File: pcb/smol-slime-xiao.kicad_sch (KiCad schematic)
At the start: 12 parts, among them J1 Conn_01x02, J2 Conn_01x02, U1 ICM-45686, U3 1532H, U4 XIAO-nRF52840-SMD

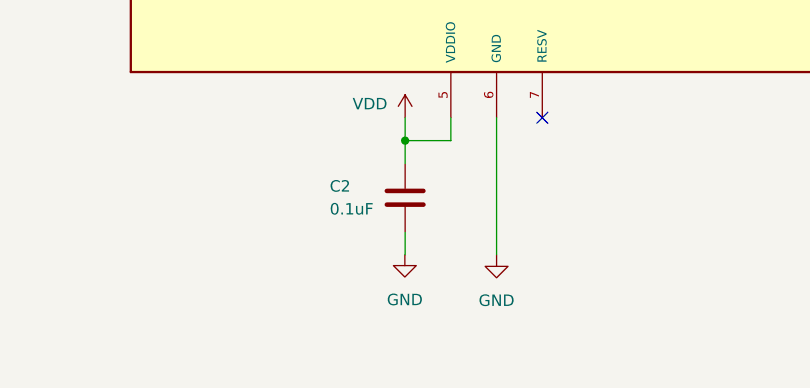
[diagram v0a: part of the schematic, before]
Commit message: Fix C2 GND connection
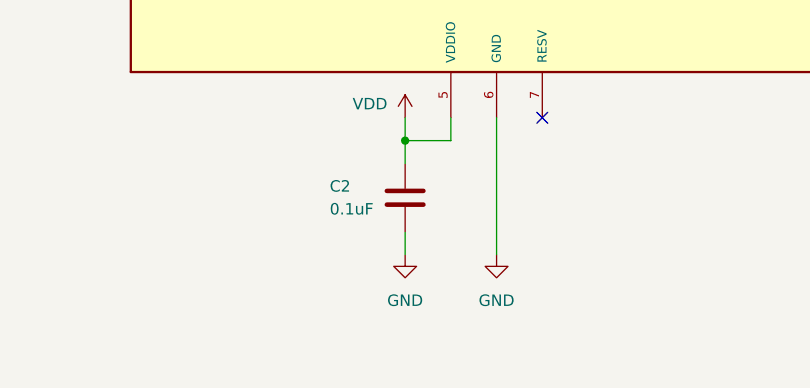
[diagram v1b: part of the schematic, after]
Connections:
- net GND: now also C2.1
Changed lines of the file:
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@@
 	(symbol
 		(lib_id "power:GND")
-		(at 69.8195 139.617 0)
+		(at 69.85 139.7 0)
 		(unit 1)
 		(exclude_from_sim no)
@@
 		(fields_autoplaced yes)
 		(property "Reference" "#PWR04"
-			(at 69.8195 145.967 0)
+			(at 69.85 146.05 0)
 			(effects
 				(font
@@
 		)
 		(property "Value" "GND"
-			(at 69.8195 144.697 0)
+			(at 69.85 144.78 0)
 			(effects
 				(font
@@
 		)
 		(property "Footprint" ""
-			(at 69.8195 139.617 0)
+			(at 69.85 139.7 0)
 			(effects
 				(font
@@
 		)
 		(property "Datasheet" ""
-			(at 69.8195 139.617 0)
+			(at 69.85 139.7 0)
 			(effects
 				(font
@@
 		)
 		(property "Description" "Power symbol creates a global label with name \"GND\" , ground"
-			(at 69.8195 139.617 0)
+			(at 69.85 139.7 0)
 			(effects
 				(font

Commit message: Add power switch
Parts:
- added SW1: Power_Switch, symbol Switch:SW_DPST_x2
- J1: value Conn_01x02 -> Battery_Terminal
- J2: value Conn_01x02 -> Charger_Connecter
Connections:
- net VBAT: now also SW1.2 (B); no longer U4.15 (BAT)
- new net: SW1.1 (A), U4.15 (BAT)
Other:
- moved on the sheet: J1
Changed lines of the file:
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@@
 	)
 	(no_connect
-		(at 226.06 86.36)
+		(at 224.79 96.52)
 	)
 	(no_connect
@@
 	(wire
 		(pts
+			(xy 231.14 87.63) (xy 231.14 91.44)
+		)
+		(stroke
+			(width 0)
+			(type default)
+		)
+	)
+	(wire
+		(pts
 			(xy 143.51 83.82) (xy 143.51 86.36)
 		)
@@
 	(wire
 		(pts
-			(xy 231.14 83.82) (xy 231.14 87.63)
+			(xy 231.14 93.98) (xy 231.14 96.52)
 		)
 		(stroke
@@
 	(wire
 		(pts
-			(xy 231.14 83.82) (xy 226.06 83.82)
+			(xy 231.14 93.98) (xy 224.79 93.98)
 		)
 		(stroke
@@
 	(wire
 		(pts
-			(xy 231.14 73.66) (xy 231.14 81.28)
+			(xy 231.14 73.66) (xy 231.14 77.47)
 		)
 		(stroke
@@
 	(wire
 		(pts
-			(xy 226.06 81.28) (xy 231.14 81.28)
+			(xy 224.79 91.44) (xy 231.14 91.44)
 		)
 		(stroke
@@
 	)
 	(label "VBAT"
-		(at 226.06 81.28 0)
+		(at 226.06 91.44 0)
 		(effects
 			(font
@@
 	(symbol
 		(lib_id "Connector_Generic:Conn_01x03")
-		(at 220.98 83.82 0)
+		(at 219.71 93.98 0)
 		(mirror y)
 		(unit 1)
@@
 		(dnp no)
 		(property "Reference" "J1"
-			(at 220.98 92.71 0)
+			(at 219.71 102.87 0)
 			(effects
 				(font
@@
 			)
 		)
-		(property "Value" "Conn_01x02"
-			(at 220.98 90.17 0)
+		(property "Value" "Battery_Terminal"
+			(at 219.71 100.33 0)
 			(effects
 				(font
@@
 		)
 		(property "Footprint" "Generic:JST_PH2_SMT"
-			(at 220.98 83.82 0)
+			(at 219.71 93.98 0)
 			(effects
 				(font
@@
 		)
 		(property "Datasheet" "~"
-			(at 220.98 83.82 0)
+			(at 219.71 93.98 0)
 			(effects
 				(font
@@
 		)
 		(property "Description" "Generic connector, single row, 01x03, script generated (kicad-library-utils/schlib/autogen/connector/)"
-			(at 220.98 83.82 0)
+			(at 219.71 93.98 0)
 			(effects
 				(font
@@
 			)
 		)
-		(property "Value" "Conn_01x02"
-			(at 252.73 90.17 0)
+		(property "Value" "Charger_Connecter"
+			(at 249.428 89.916 0)
 			(effects
 				(font
@@
 	)
 	(symbol
+		(lib_id "Switch:SW_DPST_x2")
+		(at 231.14 82.55 270)
+		(unit 1)
+		(exclude_from_sim no)
+		(in_bom yes)
+		(on_board yes)
+		(dnp no)
+		(property "Reference" "SW1"
+			(at 223.52 80.772 90)
+			(effects
+				(font
+					(size 1.27 1.27)
+				)
+				(justify left)
+			)
+		)
+		(property "Value" "Power_Switch"
+			(at 216.154 83.312 90)
+			(effects
+				(font
+					(size 1.27 1.27)
+				)
+				(justify left)
+			)
+		)
+		(property "Footprint" ""
+			(at 231.14 82.55 0)
+			(effects
+				(font
+					(size 1.27 1.27)
+				)
+				(hide yes)
+			)
+		)
+		(property "Datasheet" "~"
+			(at 231.14 82.55 0)
+			(effects
+				(font
+					(size 1.27 1.27)
+				)
+				(hide yes)
+			)
+		)
+		(property "Description" "Single Pole Single Throw (SPST) switch, separate symbol"
+			(at 231.14 82.55 0)
+			(effects
+				(font
+					(size 1.27 1.27)
+				)
+				(hide yes)
+			)
+		)
+		(pin "4"
+		)
+		(pin "3"
+		)
+		(pin "2"
+		)
+		(pin "1"
+		)
+		(instances
+			(project ""
+				(path "/d7183ea3-6ccc-4449-ab59-f8ffc6b6dac3"
+					(reference "SW1")
+					(unit 1)
+				)
+			)
+		)
+	)
+	(symbol
 		(lib_id "power:GND")
 		(at 245.11 26.67 180)
@@
 	(symbol
 		(lib_id "power:GND")
-		(at 231.14 87.63 0)
+		(at 231.14 96.52 0)
 		(unit 1)
 		(exclude_from_sim no)
@@
 		(fields_autoplaced yes)
 		(property "Reference" "#PWR018"
-			(at 231.14 93.98 0)
+			(at 231.14 102.87 0)
 			(effects
 				(font
@@
 		)
 		(property "Value" "GND"
-			(at 231.14 92.71 0)
+			(at 231.14 101.6 0)
 			(effects
 				(font
@@
 		)
 		(property "Footprint" ""
-			(at 231.14 87.63 0)
+			(at 231.14 96.52 0)
 			(effects
 				(font
@@
 		)
 		(property "Datasheet" ""
-			(at 231.14 87.63 0)
+			(at 231.14 96.52 0)
 			(effects
 				(font
@@
 		)
 		(property "Description" "Power symbol creates a global label with name \"GND\" , ground"
-			(at 231.14 87.63 0)
+			(at 231.14 96.52 0)
 			(effects
 				(font

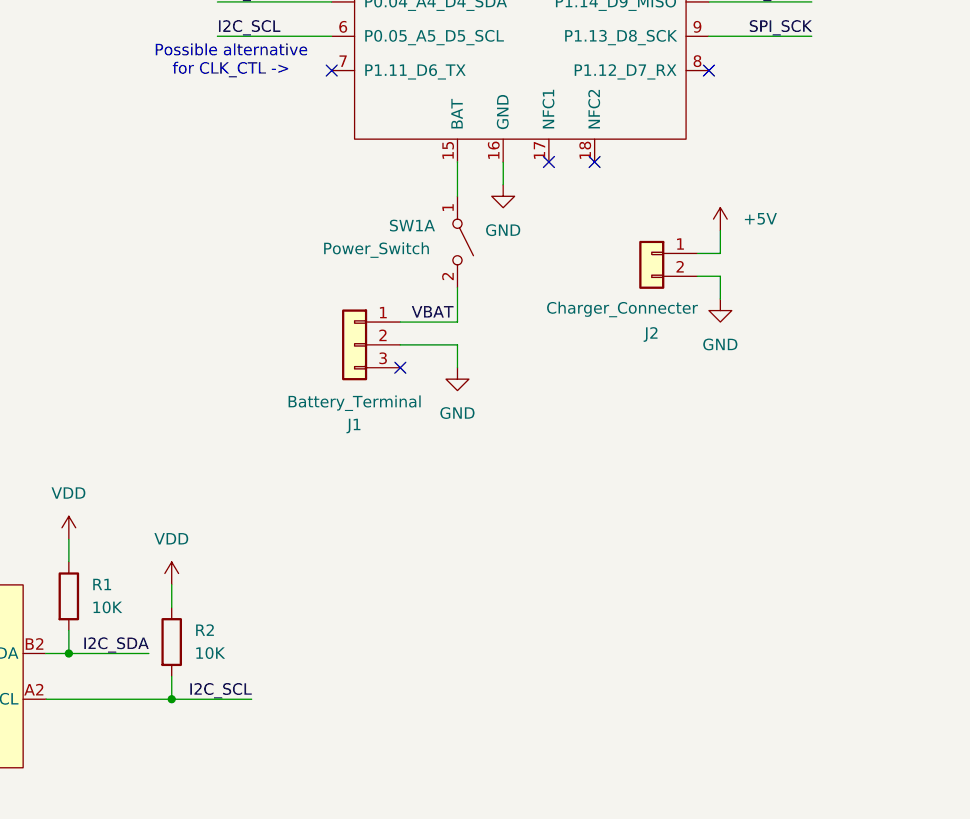
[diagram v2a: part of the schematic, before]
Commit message: Create VBAT_GND net for charge connector bypass
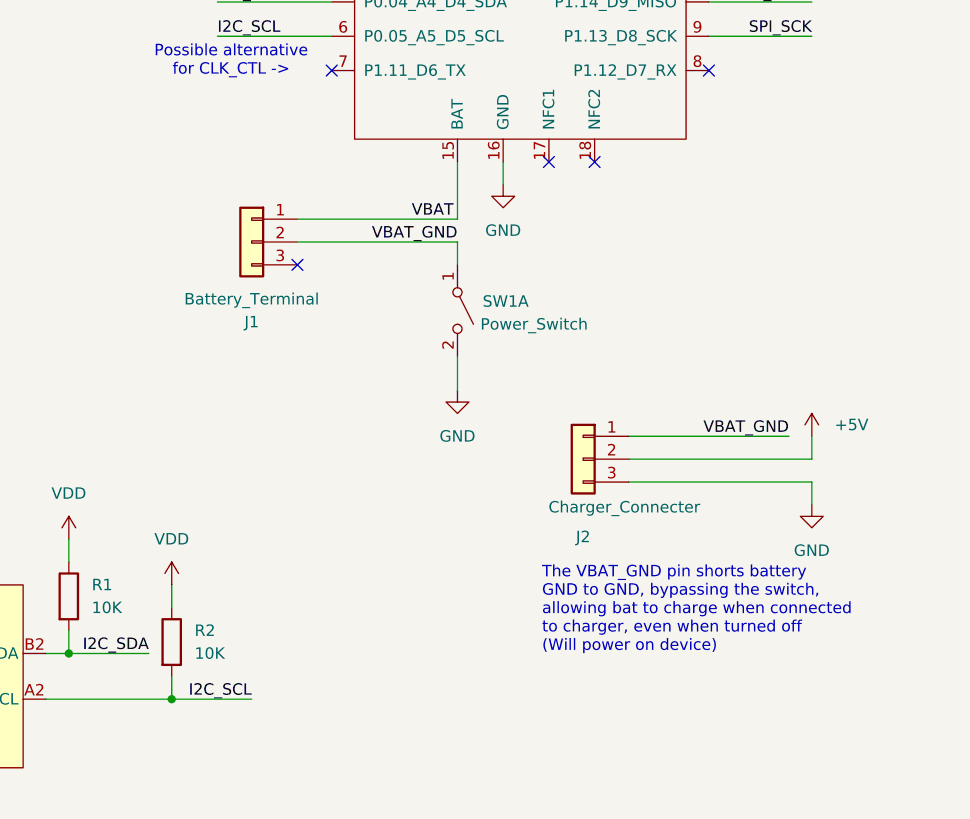
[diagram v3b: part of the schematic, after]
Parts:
- J2: symbol Connector_Generic:Conn_01x02 -> Connector_Generic:Conn_01x03
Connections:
- net +5V: now also J2.2 (Pin_2); no longer J2.1 (Pin_1)
- net GND: now also J2.3 (Pin_3), SW1.2 (B); no longer J1.2 (Pin_2), J2.2 (Pin_2)
- net VBAT: now also U4.15 (BAT); no longer SW1.2 (B)
- net VBAT_GND: now reaches SW1.1 (A)
- net VBAT_GND: now also J1.2 (Pin_2), J2.1 (Pin_1); no longer U4.15 (BAT)
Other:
- note added: "The VBAT_GND pin shorts battery GND to GND, bypassing the switch, allowing bat to charge when connected to charger, even when turned off (Will power on device)"
- moved on the sheet: J1, SW1A

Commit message: Changed charge connector footprint to 3 pin variant
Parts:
- J2: footprint Generic:PinPads_1x02_P2.54mm -> Generic:PinPads_1x03_P2.54mm
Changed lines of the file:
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@@
 			)
 		)
-		(property "Footprint" "Generic:PinPads_1x02_P2.54mm"
+		(property "Footprint" "Generic:PinPads_1x03_P2.54mm"
 			(at 245.11 106.68 0)
 			(effects

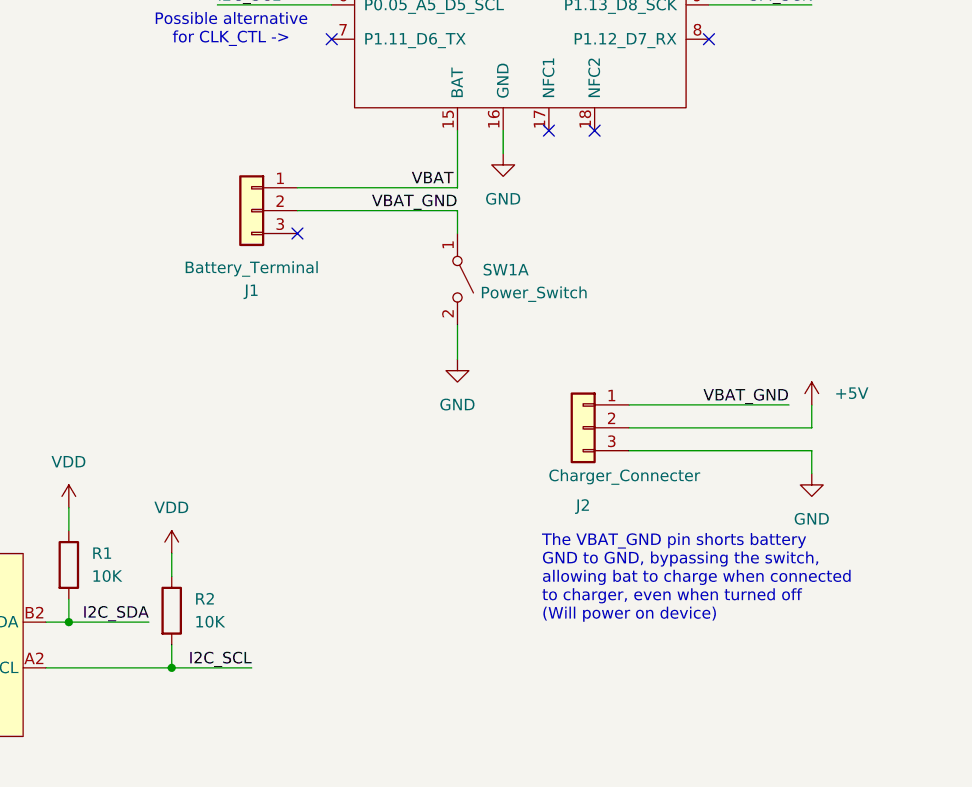
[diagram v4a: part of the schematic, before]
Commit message: Update switch symbol and circuit logic to avail parts
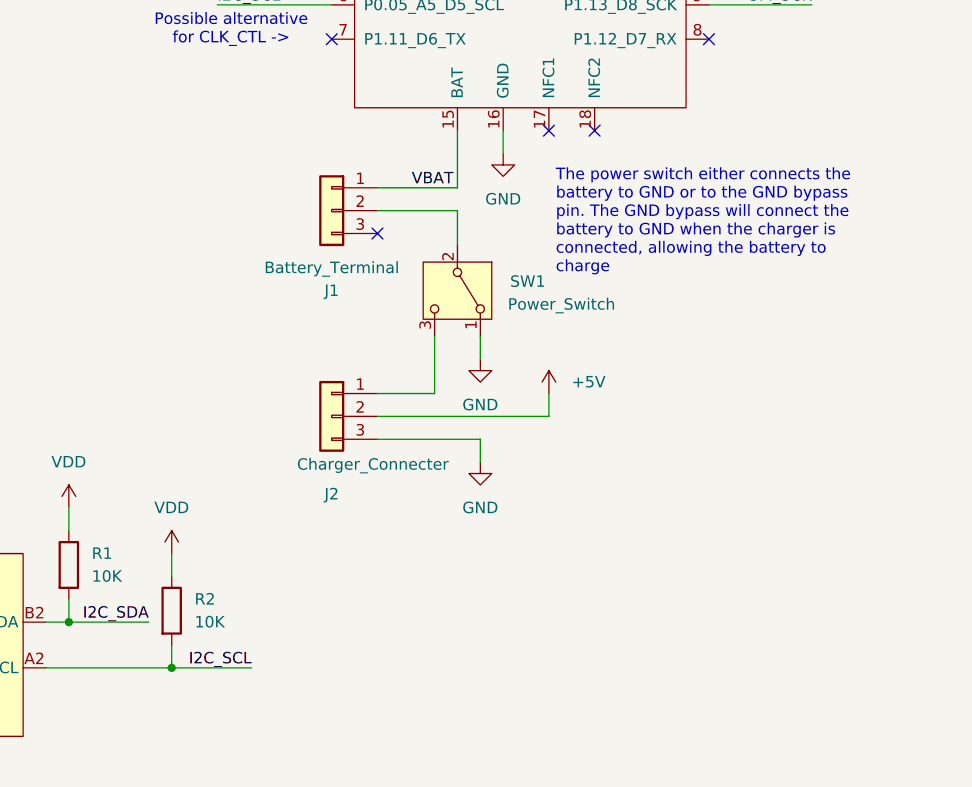
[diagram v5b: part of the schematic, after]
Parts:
- SW1: symbol Switch:SW_DPST_x2 -> Switch:SW_SPDT
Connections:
- net GND: now also SW1.1 (A); no longer SW1.2 (B)
- removed net VBAT_GND: J1.2 (Pin_2), J2.1 (Pin_1), SW1.1 (A)
- new net: J1.2 (Pin_2), SW1.2 (B)
- new net: J2.1 (Pin_1), SW1.3 (C)
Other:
- note added: "The power switch either connects the battery to GND or to the GND bypass pin. The GND bypass will connect the battery to GND when the charger is connected, allowing the battery to charge"
- note removed: "The VBAT_GND pin shorts battery GND to GND, bypassing the switch, allowing bat to charge when connected to charger, even when turned off (Will power on device)"
- moved on the sheet: J1, J2
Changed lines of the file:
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@@
 		(rev "1.0")
 	)
-	(text "The VBAT_GND pin shorts battery\nGND to GND, bypassing the switch,\nallowing bat to charge when connected\nto charger, even when turned off\n(Will power on device)"
+	(text "The power switch either connects the\nbattery to GND or to the GND bypass\npin. The GND bypass will connect the\nbattery to GND when the charger is\nconnected, allowing the battery to\ncharge"
 		(exclude_from_sim no)
-		(at 240.538 123.444 0)
+		(at 242.062 83.82 0)
 		(effects
 			(font
@@
 	)
 	(no_connect
-		(at 213.36 85.09)
+		(at 222.25 85.09)
 	)
 	(no_connect
@@
 	(wire
 		(pts
+			(xy 231.14 82.55) (xy 231.14 86.36)
+		)
+		(stroke
+			(width 0)
+			(type default)
+		)
+	)
+	(wire
+		(pts
 			(xy 187.96 115.57) (xy 187.96 118.11)
 		)
@@
 	(wire
 		(pts
-			(xy 270.51 106.68) (xy 250.19 106.68)
+			(xy 241.3 105.41) (xy 222.25 105.41)
 		)
 		(stroke
@@
 	(wire
 		(pts
-			(xy 270.51 104.14) (xy 270.51 106.68)
+			(xy 241.3 102.87) (xy 241.3 105.41)
 		)
 		(stroke
@@
 	(wire
 		(pts
-			(xy 231.14 82.55) (xy 213.36 82.55)
+			(xy 231.14 82.55) (xy 222.25 82.55)
+		)
+		(stroke
+			(width 0)
+			(type default)
+		)
+	)
+	(wire
+		(pts
+			(xy 233.68 110.49) (xy 233.68 107.95)
 		)
 		(stroke
@@
 	(wire
 		(pts
-			(xy 270.51 111.76) (xy 270.51 109.22)
+			(xy 228.6 102.87) (xy 228.6 96.52)
 		)
 		(stroke
@@
 	(wire
 		(pts
-			(xy 231.14 95.25) (xy 231.14 99.06)
+			(xy 233.68 96.52) (xy 233.68 99.06)
 		)
 		(stroke
@@
 	(wire
 		(pts
-			(xy 231.14 82.55) (xy 231.14 85.09)
-		)
-		(stroke
-			(width 0)
-			(type default)
-		)
-	)
-	(wire
-		(pts
 			(xy 96.52 30.48) (xy 85.09 30.48)
 		)
@@
 	(wire
 		(pts
-			(xy 270.51 109.22) (xy 250.19 109.22)
+			(xy 233.68 107.95) (xy 222.25 107.95)
 		)
 		(stroke
@@
 	(wire
 		(pts
-			(xy 250.19 104.14) (xy 267.97 104.14)
+			(xy 222.25 102.87) (xy 228.6 102.87)
 		)
 		(stroke
@@
 	(wire
 		(pts
-			(xy 213.36 80.01) (xy 231.14 80.01)
+			(xy 222.25 80.01) (xy 231.14 80.01)
 		)
 		(stroke
@@
 		)
 	)
-	(label "VBAT_GND"
-		(at 267.97 104.14 180)
-		(effects
-			(font
-				(size 1.27 1.27)
-			)
-			(justify right bottom)
-		)
-	)
 	(label "SPI_MISO"
 		(at 22.86 71.12 0)
@@
 		)
 	)
-	(label "VBAT_GND"
-		(at 231.14 82.55 180)
-		(effects
-			(font
-				(size 1.27 1.27)
-			)
-			(justify right bottom)
-		)
-	)
 	(label "IMU_INT"
 		(at 22.86 86.36 0)
@@
 	(symbol
 		(lib_id "power:GND")
-		(at 270.51 111.76 0)
+		(at 233.68 110.49 0)
 		(unit 1)
 		(exclude_from_sim no)
@@
 		(fields_autoplaced yes)
 		(property "Reference" "#PWR021"
-			(at 270.51 118.11 0)
+			(at 233.68 116.84 0)
 			(effects
 				(font
@@
 		)
 		(property "Value" "GND"
-			(at 270.51 116.84 0)
+			(at 233.68 115.57 0)
 			(effects
 				(font
@@
 		)
 		(property "Footprint" ""
-			(at 270.51 111.76 0)
+			(at 233.68 110.49 0)
 			(effects
 				(font
@@
 		)
 		(property "Datasheet" ""
-			(at 270.51 111.76 0)
+			(at 233.68 110.49 0)
 			(effects
 				(font
@@
 		)
 		(property "Description" "Power symbol creates a global label with name \"GND\" , ground"
-			(at 270.51 111.76 0)
+			(at 233.68 110.49 0)
 			(effects
 				(font
@@
 	(symbol
 		(lib_id "power:+5V")
-		(at 270.51 104.14 0)
+		(at 241.3 102.87 0)
 		(unit 1)
 		(exclude_from_sim no)
@@
 		(fields_autoplaced yes)
 		(property "Reference" "#PWR020"
-			(at 270.51 107.95 0)
+			(at 241.3 106.68 0)
 			(effects
 				(font
@@
 		)
 		(property "Value" "+5V"
-			(at 273.05 102.8699 0)
+			(at 243.84 101.5999 0)
 			(effects
 				(font
@@
 		)
 		(property "Footprint" ""
-			(at 270.51 104.14 0)
+			(at 241.3 102.87 0)
 			(effects
 				(font
@@
 		)
 		(property "Datasheet" ""
-			(at 270.51 104.14 0)
+			(at 241.3 102.87 0)
 			(effects
 				(font
@@
 		)
 		(property "Description" "Power symbol creates a global label with name \"+5V\""
-			(at 270.51 104.14 0)
+			(at 241.3 102.87 0)
 			(effects
 				(font
@@
 	(symbol
 		(lib_id "Connector_Generic:Conn_01x03")
-		(at 208.28 82.55 0)
+		(at 217.17 82.55 0)
 		(mirror y)
 		(unit 1)
@@
 		(dnp no)
 		(property "Reference" "J1"
-			(at 208.28 91.44 0)
+			(at 217.17 91.44 0)
 			(effects
 				(font
@@
 		)
 		(property "Value" "Battery_Terminal"
-			(at 208.28 88.9 0)
+			(at 217.17 88.9 0)
 			(effects
 				(font
@@
 		)
 		(property "Footprint" "Generic:JST_PH2_SMT"
-			(at 208.28 82.55 0)
+			(at 217.17 82.55 0)
 			(effects
 				(font
@@
 		)
 		(property "Datasheet" "~"
-			(at 208.28 82.55 0)
+			(at 217.17 82.55 0)
 			(effects
 				(font
@@
 		)
 		(property "Description" "Generic connector, single row, 01x03, script generated (kicad-library-utils/schlib/autogen/connector/)"
-			(at 208.28 82.55 0)
+			(at 217.17 82.55 0)
 			(effects
 				(font
@@
 	(symbol
 		(lib_id "Connector_Generic:Conn_01x03")
-		(at 245.11 106.68 0)
+		(at 217.17 105.41 0)
 		(mirror y)
 		(unit 1)
@@
 		(dnp no)
 		(property "Reference" "J2"
-			(at 245.11 115.316 0)
+			(at 217.17 114.046 0)
 			(effects
 				(font
@@
 		)
 		(property "Value" "Charger_Connecter"
-			(at 249.682 112.014 0)
+			(at 221.742 110.744 0)
 			(effects
 				(font
@@
 		)
 		(property "Footprint" "Generic:PinPads_1x03_P2.54mm"
-			(at 245.11 106.68 0)
+			(at 217.17 105.41 0)
 			(effects
 				(font
@@
 		)
 		(property "Datasheet" "~"
-			(at 245.11 106.68 0)
+			(at 217.17 105.41 0)
 			(effects
 				(font
@@
 		)
 		(property "Description" "Generic connector, single row, 01x03, script generated (kicad-library-utils/schlib/autogen/connector/)"
-			(at 245.11 106.68 0)
+			(at 217.17 105.41 0)
 			(effects
 				(font
@@
 	)
 	(symbol
-		(lib_id "Switch:SW_DPST_x2")
-		(at 231.14 90.17 270)
+		(lib_id "Switch:SW_SPDT")
+		(at 231.14 91.44 270)
 		(unit 1)
 		(exclude_from_sim no)
@@
 		(dnp no)
 		(property "Reference" "SW1"
-			(at 233.934 89.154 90)
+			(at 236.982 90.424 90)
 			(effects
 				(font
@@
 		)
 		(property "Value" "Power_Switch"
-			(at 233.68 91.694 90)
+			(at 236.728 92.964 90)
 			(effects
 				(font
@@
 		)
 		(property "Footprint" ""
-			(at 231.14 90.17 0)
+			(at 231.14 91.44 0)
 			(effects
 				(font
@@
 		)
 		(property "Datasheet" "~"
-			(at 231.14 90.17 0)
+			(at 223.52 91.44 0)
 			(effects
 				(font
@@
 			)
 		)
-		(property "Description" "Single Pole Single Throw (SPST) switch, separate symbol"
-			(at 231.14 90.17 0)
+		(property "Description" "Switch, single pole double throw"
+			(at 231.14 91.44 0)
 			(effects
 				(font
@@
 			)
 		)
-		(pin "4"
-		)
 		(pin "3"
 		)
@@
 	(symbol
 		(lib_id "power:GND")
-		(at 231.14 99.06 0)
+		(at 233.68 99.06 0)
 		(unit 1)
 		(exclude_from_sim no)
@@
 		(fields_autoplaced yes)
 		(property "Reference" "#PWR018"
-			(at 231.14 105.41 0)
+			(at 233.68 105.41 0)
 			(effects
 				(font
@@
 		)
 		(property "Value" "GND"
-			(at 231.14 104.14 0)
+			(at 233.68 104.14 0)
 			(effects
 				(font
@@
 		)
 		(property "Footprint" ""
-			(at 231.14 99.06 0)
+			(at 233.68 99.06 0)
 			(effects
 				(font
@@
 		)
 		(property "Datasheet" ""
-			(at 231.14 99.06 0)
+			(at 233.68 99.06 0)
 			(effects
 				(font
@@
 		)
 		(property "Description" "Power symbol creates a global label with name \"GND\" , ground"
-			(at 231.14 99.06 0)
+			(at 233.68 99.06 0)
 			(effects
 				(font

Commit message: Add power switch
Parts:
- SW1: footprint (none) -> SW_SSSS811101:SW_SSSS811101
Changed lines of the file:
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@@
 			)
 		)
-		(property "Footprint" ""
-			(at 231.14 91.44 0)
+		(property "Footprint" "SW_SSSS811101:SW_SSSS811101"
+			(at 253.238 95.25 90)
 			(effects
 				(font
 					(size 1.27 1.27)
 				)
-				(hide yes)
 			)
 		)
-		(property "Datasheet" "~"
+		(property "Datasheet" "https://jlcpcb.com/partdetail/ALPSALPINE-SSSS811101/C109335"
 			(at 223.52 91.44 0)
 			(effects
